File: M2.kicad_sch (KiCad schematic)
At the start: 59 parts, among them J100 Bus_M.2_2199230-2, J6 Bus_M.2_1-2199230-6, Y1 Oscillator_32.768kHz_ECS_2520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

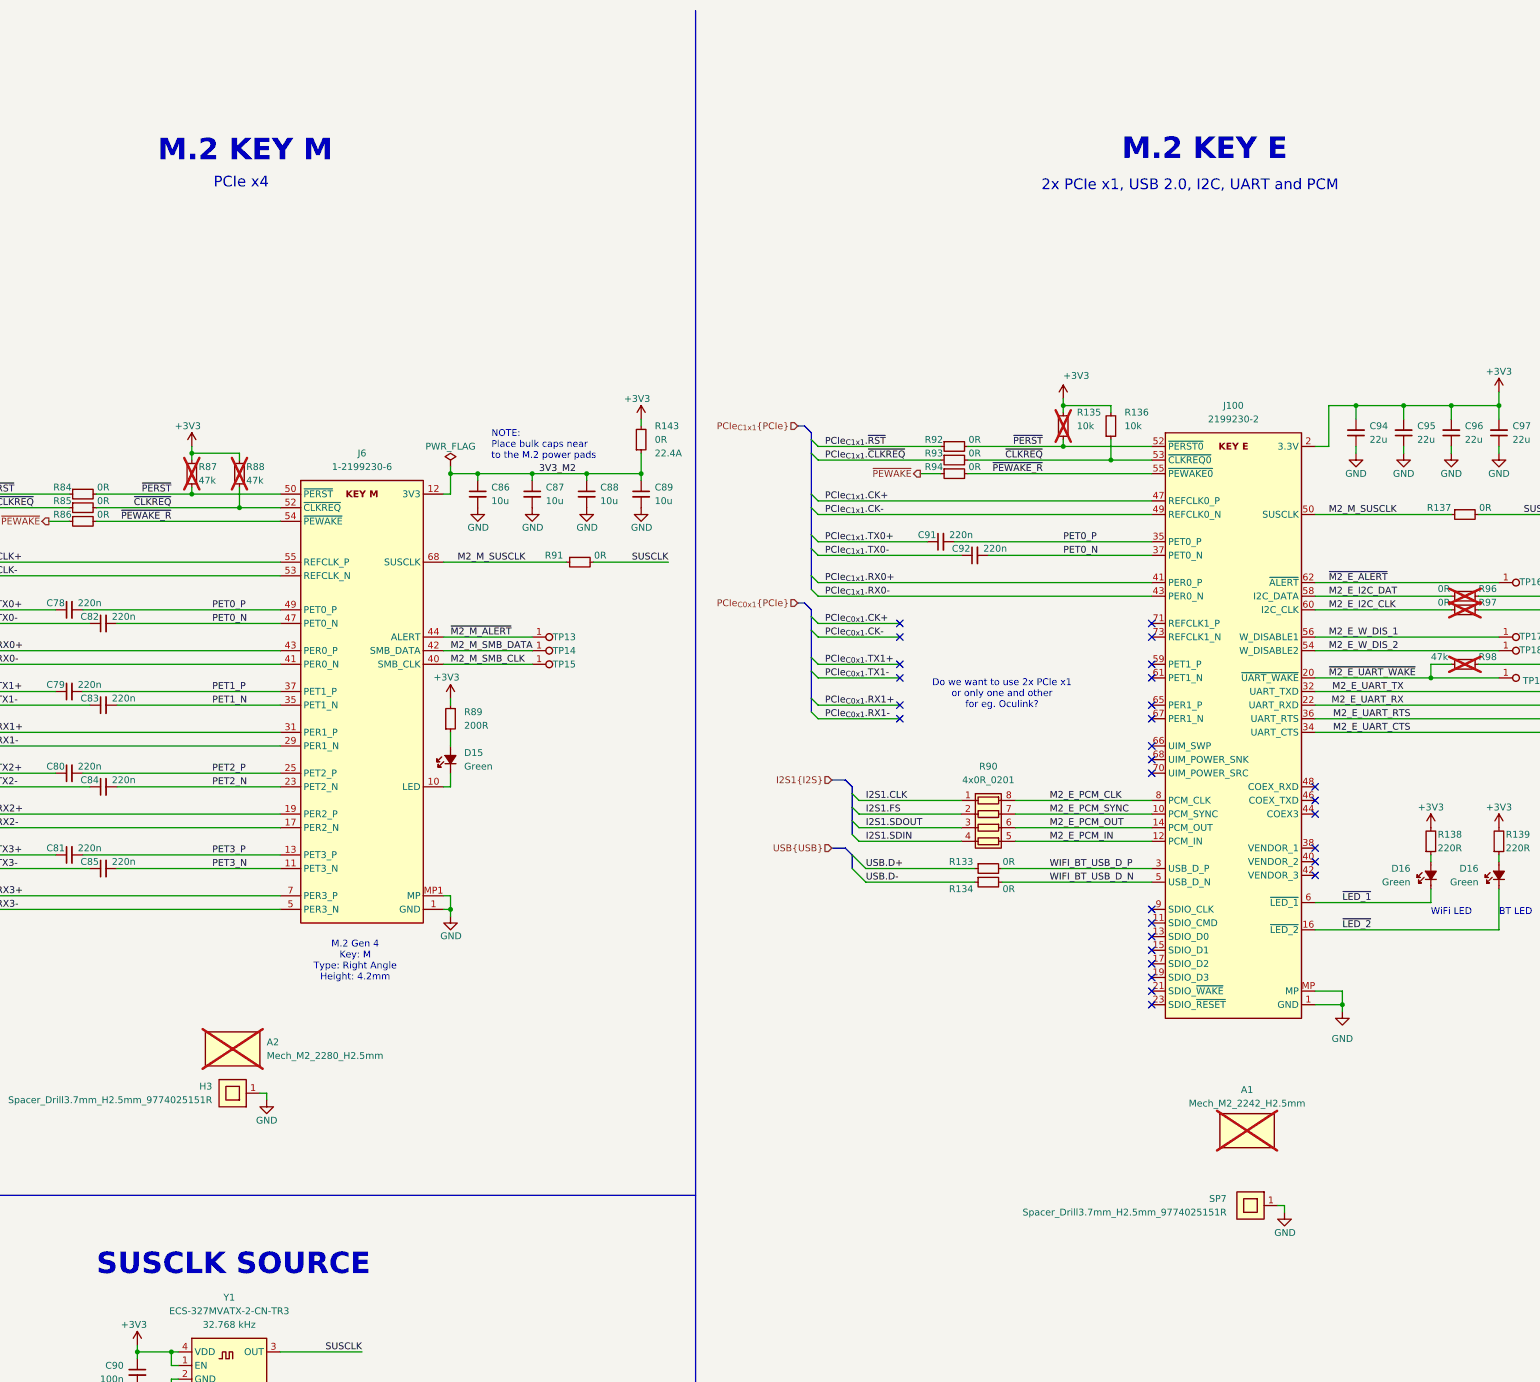
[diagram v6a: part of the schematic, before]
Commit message: [#82054] Rebase CSI branch
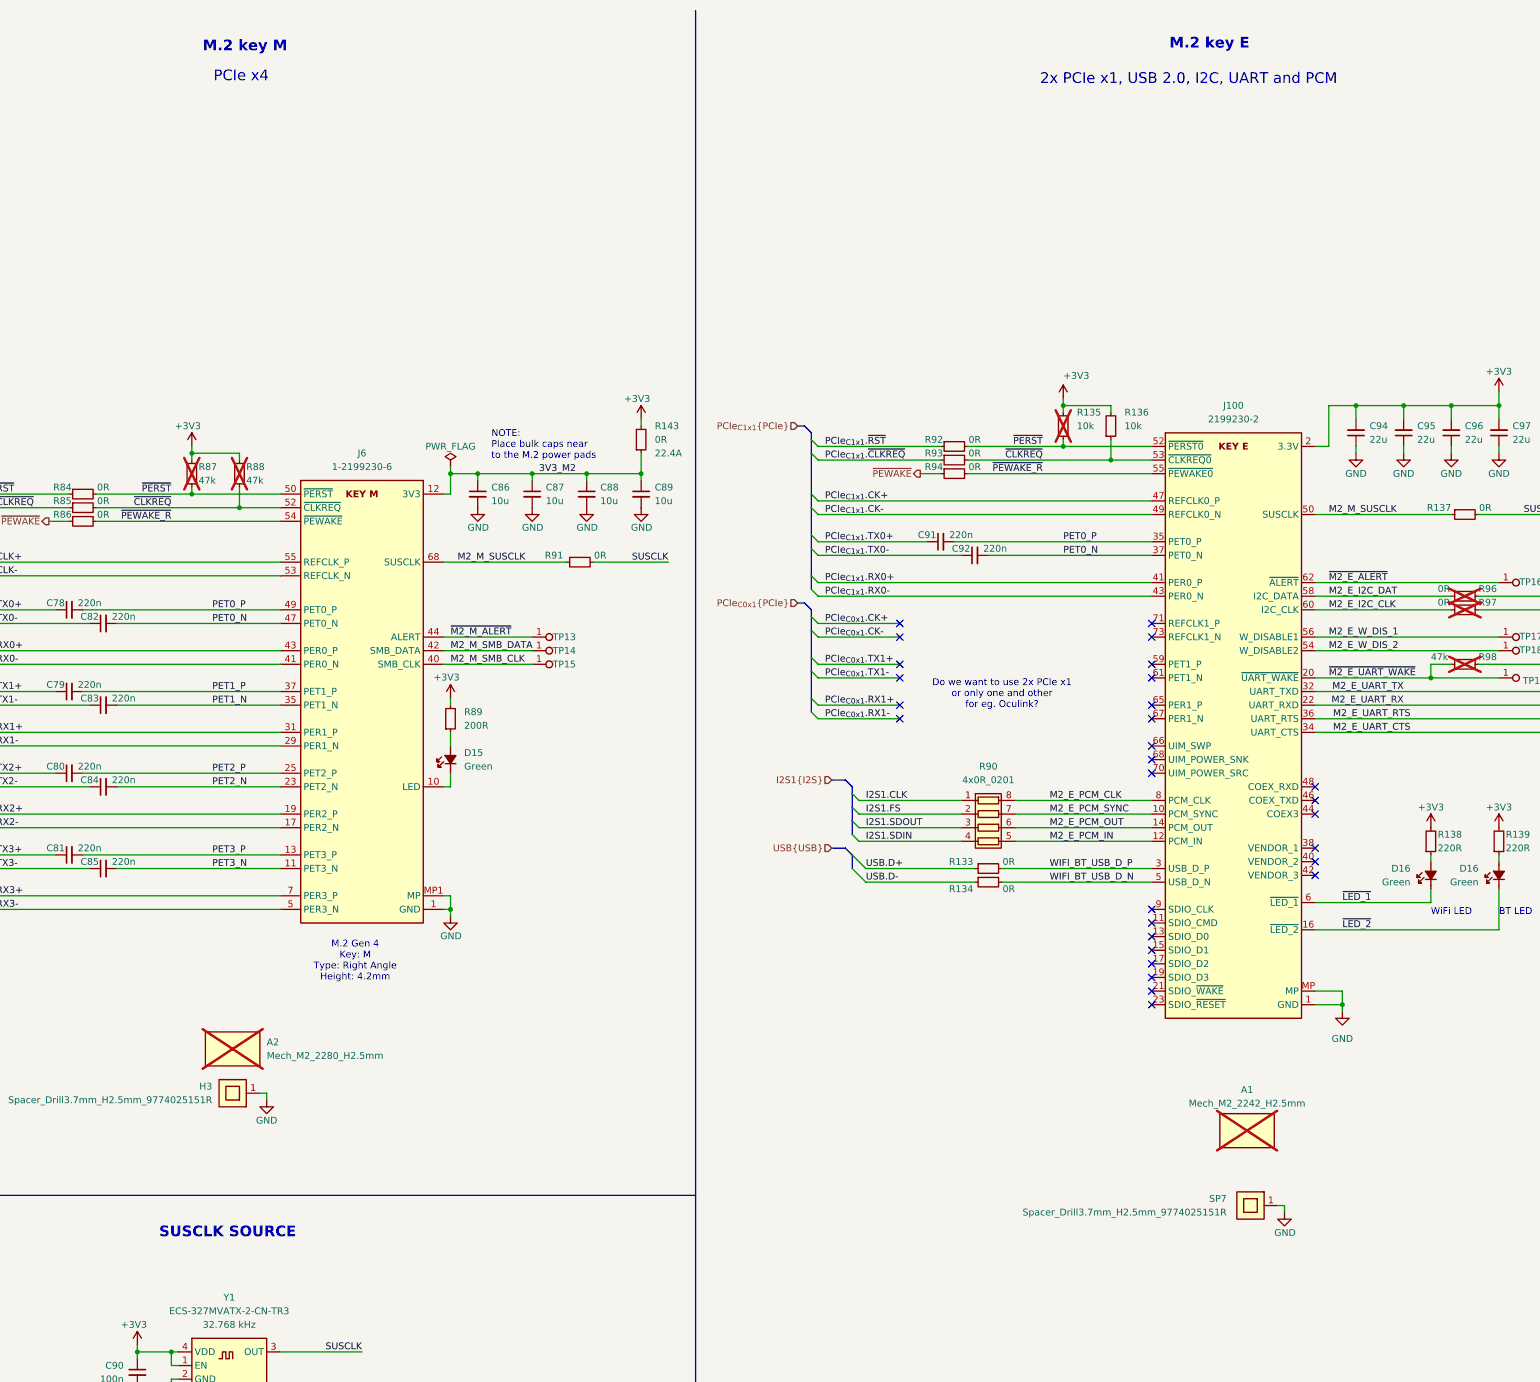
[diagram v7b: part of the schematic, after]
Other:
- note added: "M.2 key E"
- note added: "M.2 key M"
- note removed: "M.2 KEY E"
- note removed: "M.2 KEY M"
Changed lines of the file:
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@@
 	)
 	(bus_alias "CSI"
-		(members "D0+" "D0-" "D1+" "D1-" "CLK+" "CLK-")
+		(members "D0+" "D0-" "D1+" "D1-" "D2+" "D2-" "D3+" "D3-" "CLK+" "CLK-")
 	)
 	(bus_alias "DP"
@@
 		(members "TX+" "TX-" "RX+" "RX-")
 	)
-	(text "M.2 KEY M"
-		(exclude_from_sim no)
-		(at 77.47 41.148 0)
-		(effects
-			(font
-				(size 4 4)
-				(thickness 0.8)
-				(bold yes)
-			)
-			(justify left bottom)
-		)
-	)
 	(text "Do we want to use 2x PCIe x1\nor only one and other \nfor eg. Oculink?"
 		(exclude_from_sim no)
@@
 				(size 1.27 1.27)
 			)
+		)
+	)
+	(text "M.2 key E"
+		(exclude_from_sim no)
+		(at 266.192 20.066 0)
+		(effects
+			(font
+				(size 2 2)
+				(thickness 0.508)
+				(bold yes)
+			)
+			(justify left bottom)
+		)
+	)
+	(text "M.2 key M"
+		(exclude_from_sim no)
+		(at 85.852 20.574 0)
+		(effects
+			(font
+				(size 2 2)
+				(thickness 0.508)
+				(bold yes)
+			)
+			(justify left bottom)
 		)
 	)
@@
 	(text "2x PCIe x1, USB 2.0, I2C, UART and PCM"
 		(exclude_from_sim no)
-		(at 242.316 46.482 0)
+		(at 242.062 26.67 0)
 		(effects
 			(font
@@
 		)
 	)
-	(text "M.2 KEY E"
+	(text "SUSCLK SOURCE"
 		(exclude_from_sim no)
-		(at 257.302 40.894 0)
+		(at 77.724 241.808 0)
 		(effects
 			(font
-				(size 4 4)
-				(thickness 0.8)
+				(size 2 2)
+				(thickness 0.508)
 				(bold yes)
 			)
@@
 				(size 1.27 1.27)
 			)
-		)
-	)
-	(text "SUSCLK SOURCE"
-		(exclude_from_sim no)
-		(at 66.04 248.92 0)
-		(effects
-			(font
-				(size 4 4)
-				(thickness 0.8)
-				(bold yes)
-			)
-			(justify left bottom)
 		)
 	)
@@
 	(text "PCIe x4"
 		(exclude_from_sim no)
-		(at 87.884 45.974 0)
+		(at 87.884 26.162 0)
 		(effects
 			(font

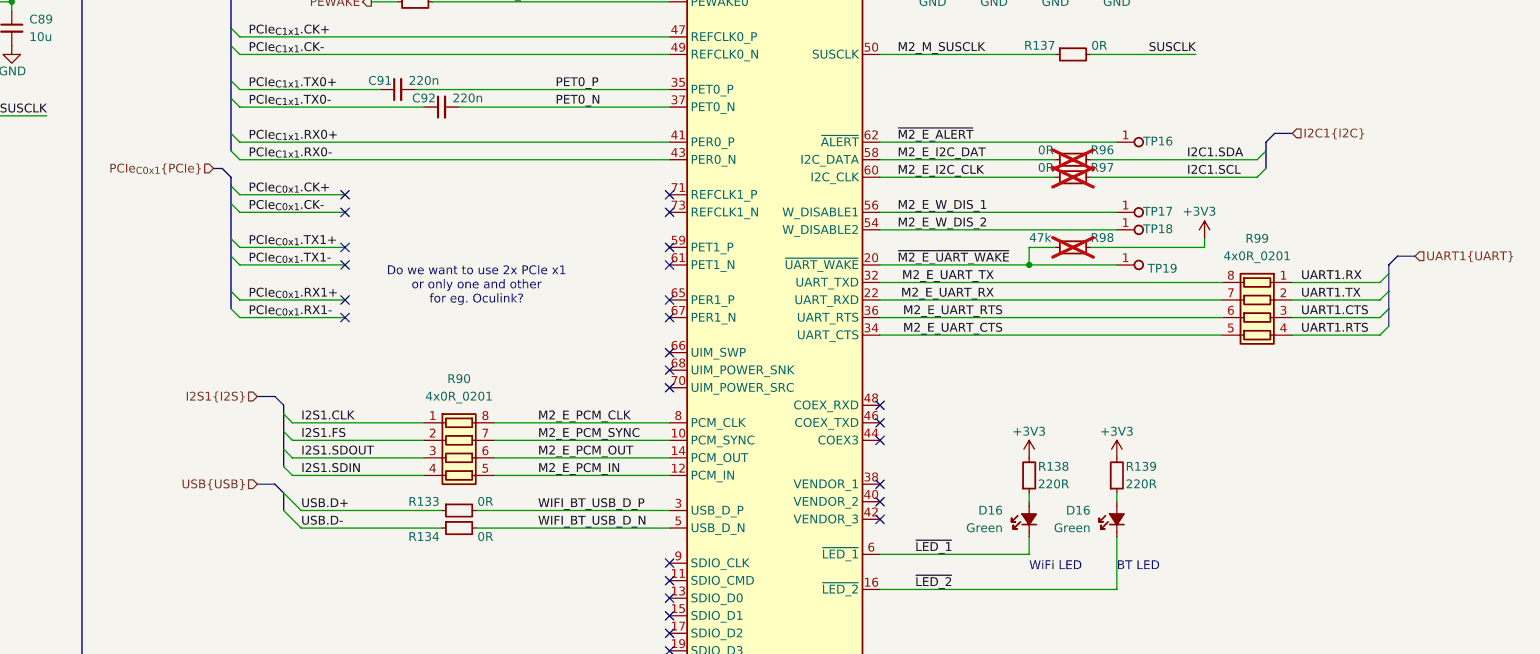
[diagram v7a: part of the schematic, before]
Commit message: [#81970] Route traces from root schematic on other schematics
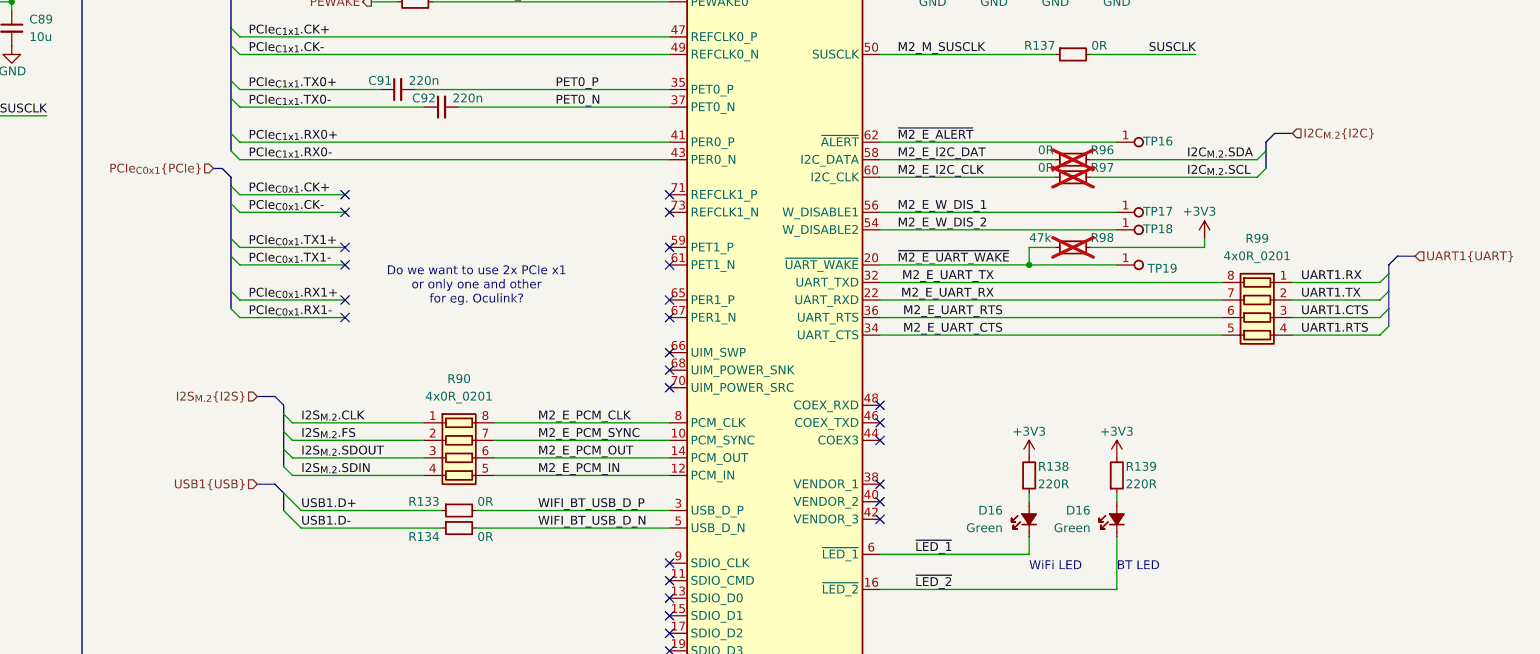
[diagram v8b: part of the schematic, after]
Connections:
- net I2C1.SCL renamed I2C_{M.2}.SCL
- net I2C1.SDA renamed I2C_{M.2}.SDA
- net I2S1.CLK renamed I2S_{M.2}.CLK
- net I2S1.FS renamed I2S_{M.2}.FS
- net I2S1.SDIN renamed I2S_{M.2}.SDIN
- net I2S1.SDOUT renamed I2S_{M.2}.SDOUT
- net USB.D+ renamed USB1.D+
- net USB.D- renamed USB1.D-
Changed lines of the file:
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@@
 		(members "D+" "D-")
 	)
-	(bus_alias "USBSS"
-		(members "TX+" "TX-" "RX+" "RX-")
-	)
 	(text "Do we want to use 2x PCIe x1\nor only one and other \nfor eg. Oculink?"
 		(exclude_from_sim no)
@@
 		)
 	)
-	(label "I2S1.SDIN"
+	(label "I2S_{M.2}.SDIN"
 		(at 209.55 167.64 0)
 		(effects
@@
 		)
 	)
-	(label "I2S1.CLK"
+	(label "I2S_{M.2}.CLK"
 		(at 209.55 160.02 0)
 		(effects
@@
 		)
 	)
-	(label "I2C1.SCL"
+	(label "I2C_{M.2}.SCL"
 		(at 337.82 124.46 0)
 		(effects
@@
 		)
 	)
-	(label "USB.D-"
+	(label "USB1.D-"
 		(at 209.55 175.26 0)
 		(effects
@@
 		)
 	)
-	(label "I2C1.SDA"
+	(label "I2C_{M.2}.SDA"
 		(at 337.82 121.92 0)
 		(effects
@@
 		)
 	)
-	(label "USB.D+"
+	(label "USB1.D+"
 		(at 209.55 172.72 0)
 		(effects
@@
 		)
 	)
-	(label "I2S1.FS"
+	(label "I2S_{M.2}.FS"
 		(at 209.55 162.56 0)
 		(effects
@@
 		)
 	)
-	(label "I2S1.SDOUT"
+	(label "I2S_{M.2}.SDOUT"
 		(at 209.55 165.1 0)
 		(effects
@@
 		)
 	)
-	(hierarchical_label "I2C1{I2C}"
+	(hierarchical_label "I2C_{M.2}{I2C}"
 		(shape input)
 		(at 353.06 118.11 0)
@@
 		)
 	)
-	(hierarchical_label "I2S1{I2S}"
+	(hierarchical_label "I2S_{M.2}{I2S}"
 		(shape input)
 		(at 203.2 156.21 180)
@@
 		)
 	)
-	(hierarchical_label "USB{USB}"
+	(hierarchical_label "USB1{USB}"
 		(shape input)
 		(at 203.2 168.91 180)
